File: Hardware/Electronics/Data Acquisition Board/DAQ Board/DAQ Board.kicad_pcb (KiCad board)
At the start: 4 copper layers, 94.7 x 58.9 mm, 131 parts, among them J1 Conn_01x09_Male, J2 USB_B_Mini, J3 Battery Connector, J4 DC Barrel Jack, J5 HC-05 BT Module, J6 ICSP Header, Q1 DMP2100U, SW1 DIP, SW10 SW_SPDT, SW11 SW_SPDT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

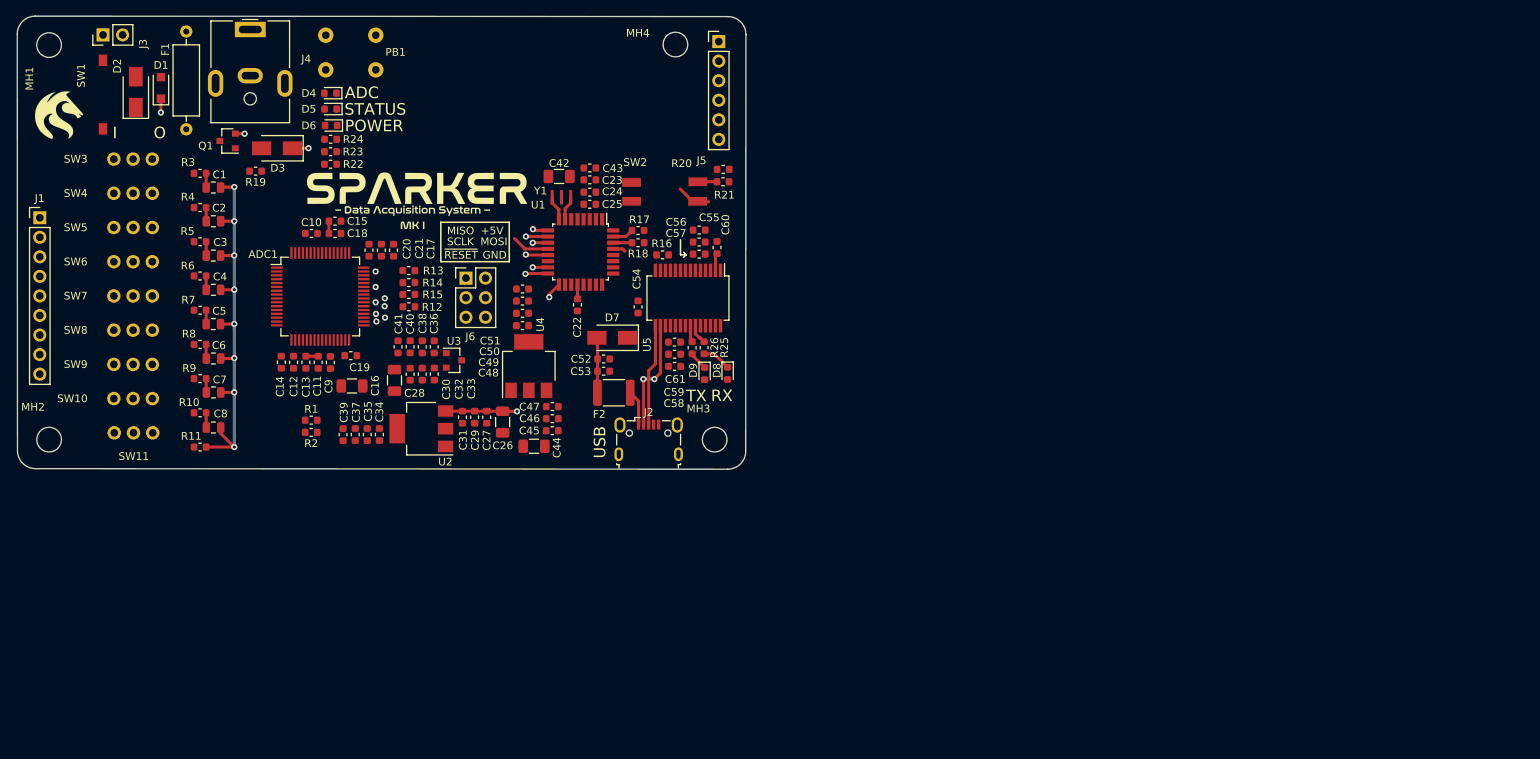
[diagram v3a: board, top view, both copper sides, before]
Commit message: About to start routing traces
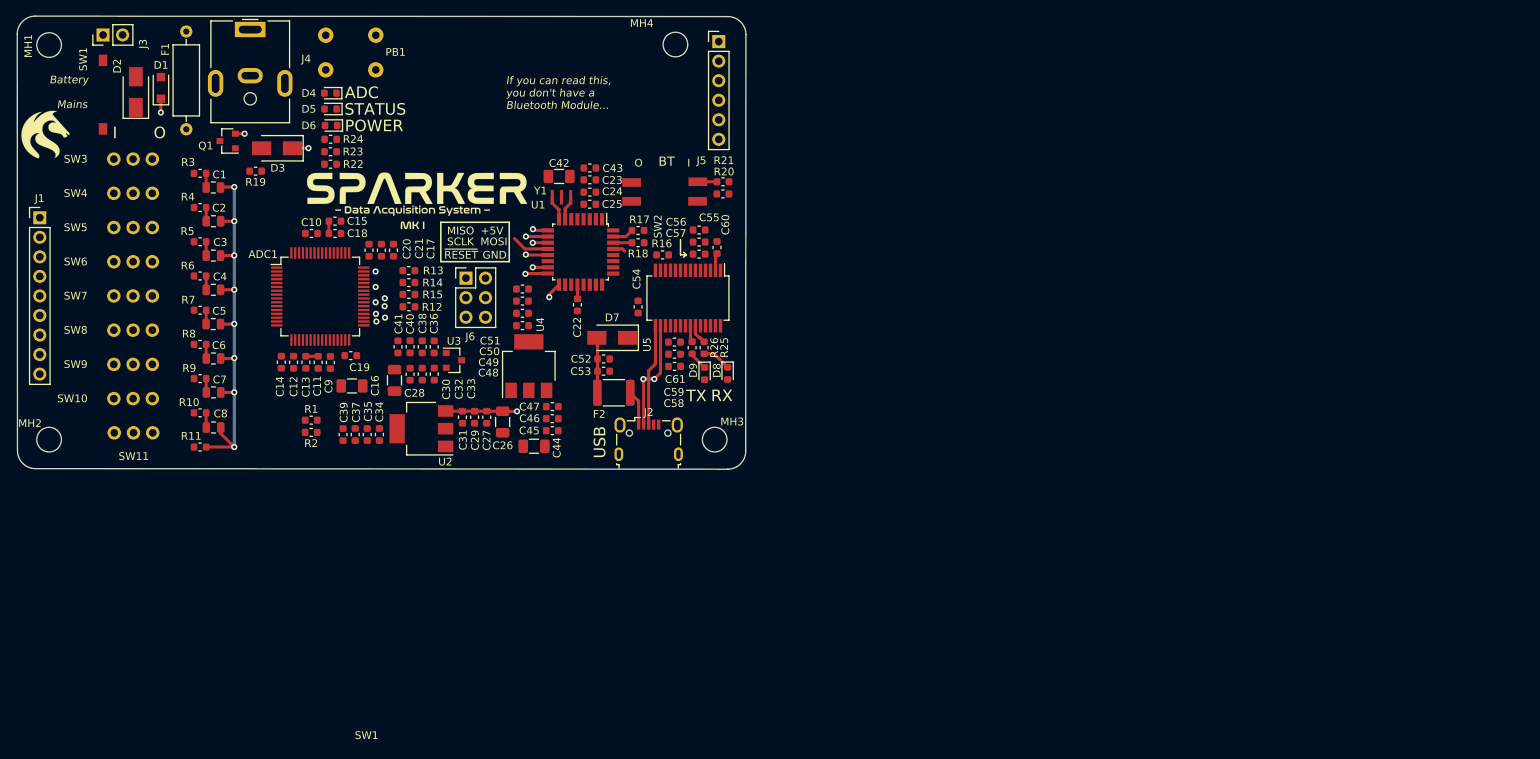
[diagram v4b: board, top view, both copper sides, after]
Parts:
- added ?: , , F.Cu at (24.7, 74.8)
- moved R20 3.19 mm to (110.4, 88.5)
- moved LOGO1 3.08 mm to (22.3, 80.9)
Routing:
- net /HC05_TX: track 2.90 -> 0.00 mm
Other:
- board text added: "BT"
- board text added: "Battery"
- board text added: "If you can read this, you don't have a Bluetooth Module..."
- board text added: "Mains"
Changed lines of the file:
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@@
   (general
     (thickness 1.6)
-    (drawings 31)
-    (tracks 152)
+    (drawings 37)
+    (tracks 150)
     (zones 0)
-    (modules 131)
+    (modules 132)
     (nets 115)
   )
@@
     (visible_elements 7FFFF7FF)
     (pcbplotparams
-      (layerselection 0x010fc_ffffffff)
+      (layerselection 0x090fc_fffffff9)
       (usegerberextensions false)
       (usegerberattributes false)
@@
       (padsonsilk false)
       (subtractmaskfromsilk false)
-      (outputformat 1)
+      (outputformat 4)
       (mirror false)
-      (drillshape 1)
+      (drillshape 0)
       (scaleselection 1)
-      (outputdirectory ""))
+      (outputdirectory "PDFs/"))
   )
   (net 0 "")
@@
     (add_net "Net-(U5-Pad9)")
   )
+  (module "" (layer F.Cu)
+    (at 24.71 74.85)
+    (fp_text reference "" (at 36.25 83.995) (layer F.SilkS)
+      (effects (font (size 1.27 1.27) (thickness 0.15)))
+    )
+    (fp_text value "" (at 36.25 83.995) (layer F.SilkS)
+      (effects (font (size 1.27 1.27) (thickness 0.15)))
+    )
+    (fp_text user SW1 (at 39.38 84.015) (layer F.SilkS)
+      (effects (font (size 1 1) (thickness 0.15)))
+    )
+  )
   (module Switches:SPDT-THT_Slide (layer F.Cu)
     (at 36.25 83.995 180)
@@
     (tags "mounting hole 3.2mm no annular m3")
     (attr virtual)
-    (fp_text reference MH4 (at -4.88 -1.49) (layer F.SilkS)
+    (fp_text reference MH4 (at -4.38 -2.75) (layer F.SilkS)
       (effects (font (size 1 1) (thickness 0.15)))
     )
@@
     (tags "mounting hole 3.2mm no annular m3")
     (attr virtual)
-    (fp_text reference MH3 (at -2.11 -4.01) (layer F.SilkS)
+    (fp_text reference MH3 (at 2.27 -2.32) (layer F.SilkS)
       (effects (font (size 1 1) (thickness 0.15)))
     )
@@
     (tags "mounting hole 3.2mm no annular m3")
     (attr virtual)
-    (fp_text reference MH2 (at -2.09 -4.22) (layer F.SilkS)
+    (fp_text reference MH2 (at -2.48 -2.1) (layer F.SilkS)
       (effects (font (size 1 1) (thickness 0.15)))
     )
@@
     (tags "mounting hole 3.2mm no annular m3")
     (attr virtual)
-    (fp_text reference MH1 (at -2.53 4.37 90) (layer F.SilkS)
+    (fp_text reference MH1 (at -2.68 0.13 90) (layer F.SilkS)
       (effects (font (size 1 1) (thickness 0.15)))
     )
@@
   )
   (module Sparker:UoN (layer F.Cu)
-    (at 24.1 78.34)
+    (at 22.34 80.87)
     (fp_text reference LOGO1 (at 0 0) (layer F.SilkS) hide
       (effects (font (size 1.524 1.524) (thickness 0.3)))
@@
   (module Switches:DIP-Switch_01x01 (layer F.Cu)
     (at 29.84 80.07 90)
-    (fp_text reference SW1 (at 6.93 -2.82 90) (layer F.SilkS)
+    (fp_text reference SW1 (at 9.05 -2.55 90) (layer F.SilkS)
       (effects (font (size 1 1) (thickness 0.15)))
     )
@@
   (module Switches:DIP-Switch_01x02 (layer F.Cu)
     (at 98.512327 86.936407)
-    (fp_text reference SW2 (at 0.47 -2.52) (layer F.SilkS)
+    (fp_text reference SW2 (at 3.437673 5.803593 90) (layer F.SilkS)
       (effects (font (size 1 1) (thickness 0.15)))
     )
@@
   )
   (module Resistor_SMD:R_0603_1608Metric (layer F.Cu)
-    (at 110.41 85.33)
+    (at 110.38 88.52)
     (descr "Resistor SMD 0603 (1608 Metric), square (rectangular) end terminal, IPC_7351 nominal, (Body size source: http://www.tortai-tech.com/upload/download/2011102023233369053.pdf), generated with kicad-footprint-generator")
     (tags resistor)
     (attr smd)
-    (fp_text reference R20 (at -5.4 -0.77) (layer F.SilkS)
+    (fp_text reference R20 (at 0.14 -2.88 180) (layer F.SilkS)
       (effects (font (size 1 1) (thickness 0.15)))
     )
@@
     (tags resistor)
     (attr smd)
-    (fp_text reference R21 (at -0.177673 -1.713593 180) (layer F.SilkS)
+    (fp_text reference R21 (at -0.107673 2.766407 180) (layer F.SilkS)
       (effects (font (size 1 1) (thickness 0.15)))
     )
@@
       (net 89 "Net-(U1-Pad7)"))
   )
+  (gr_text BT (at 101.99 84.31) (layer F.SilkS)
+    (effects (font (size 1.2 1.2) (thickness 0.2)) (justify left))
+  )
+  (gr_text O (at 98.88 84.5) (layer F.SilkS)
+    (effects (font (size 1 1) (thickness 0.15)) (justify left))
+  )
+  (gr_text I (at 105.74 84.5) (layer F.SilkS)
+    (effects (font (size 1 1) (thickness 0.15)) (justify left))
+  )
+  (gr_text Mains (at 27.84 76.9) (layer F.SilkS)
+    (effects (font (size 1 1) (thickness 0.15) italic) (justify right))
+  )
+  (gr_text Battery (at 27.95 73.69) (layer F.SilkS)
+    (effects (font (size 1 1) (thickness 0.15) italic) (justify right))
+  )
+  (gr_text "If you can read this, \nyou don't have a\nBluetooth Module..." (at 82.19 75.4) (layer F.SilkS)
+    (effects (font (size 1 1) (thickness 0.15) italic) (justify left))
+  )
   (gr_line (start 73.73 97.32) (end 82.62 97.32) (layer F.SilkS) (width 0.2))
   (gr_line (start 73.73 92.2) (end 73.73 97.32) (layer F.SilkS) (width 0.2))
@@
   (segment (start 89.08 90.53) (end 89.03 90.53) (width 0.4) (layer F.Cu) (net 90))
   (segment (start 89.08 91.81) (end 89.08 90.53) (width 0.4) (layer F.Cu) (net 90))
-  (segment (start 107.857327 89.536407) (end 108.512327 89.536407) (width 0.4) (layer F.Cu) (net 112))
-  (segment (start 104.839999 87.889079) (end 106.427327 89.476407) (width 0.4) (layer F.Cu) (net 112))
 )

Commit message: Kineses Board layout finished, about to start routing
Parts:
- removed ?: , 
- moved C17 3.22 mm to (64.4, 95.8)
- moved C44 3.05 mm to (88.9, 121.3), turned to 0 degrees
- moved C20 1.54 mm to (65.9, 95.8)
- moved C21 1.54 mm to (67.5, 95.8)
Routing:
- net Net-(J1-Pad9): track 0.00 -> 13.9 mm
- net Net-(J1-Pad1): track 0.00 -> 13.5 mm
- net Net-(J1-Pad8): track 0.08 -> 12.1 mm
- net Net-(J1-Pad2): track 0.00 -> 12.0 mm
- net Net-(J1-Pad7): track 0.00 -> 11.2 mm
- net Net-(J1-Pad3): track 0.00 -> 11.2 mm
- net /ADC1299/AVDD: track 0.00 -> 11.0 mm
- net Net-(D4-Pad2): track 0.00 -> 10.9 mm
- net /VIN_RAW: track 0.00 -> 10.7 mm
- net Net-(J1-Pad6): track 0.00 -> 10.4 mm
- net Net-(J1-Pad4): track 0.00 -> 10.4 mm
- net Net-(J1-Pad5): track 0.00 -> 9.62 mm
- net Net-(R7-Pad2): track 0.00 -> 8.69 mm
- net Net-(R5-Pad2): track 0.00 -> 8.69 mm
- net Net-(R6-Pad2): track 0.00 -> 8.69 mm
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- added copper zone on In1.Cu, net /GND
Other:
- net class Default: clearance 0.2 -> 0.15; trace_width 0.4 -> 0.3
- net class High_Current added: clearance 0.2, trace_width 0.8, via_dia 1, via_drill 0.8
- rule trace_clearance: 0.2 -> 0.15

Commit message: Routing Finished
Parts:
- moved C21 101.3 mm to (168.8, 99.0)
- moved C20 101.3 mm to (167.2, 99.0)
- moved C11 99.9 mm to (157.6, 113.6)
- moved C28 99.9 mm to (167.5, 115.9)
- moved C30 99.9 mm to (169.6, 115.1)
- moved C40 99.9 mm to (169.6, 111.6)
- moved C45 99.9 mm to (188.0, 122.5)
- moved C55 99.9 mm to (207.1, 96.4)
- moved C56 99.9 mm to (207.1, 98.0)
- moved C57 99.9 mm to (207.1, 99.5)
- moved D8 99.9 mm to (210.8, 115.0)
- moved J2 99.9 mm to (200.5, 123.6)
- moved J6 99.9 mm to (176.8, 102.7)
- moved MH4 99.9 mm to (204.0, 72.3)
- moved ADC1 99.9 mm to (157.9, 105.0)
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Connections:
- J5 pad 1: /AT_COMM -> Net-(J5-Pad1)
- U1 pad 32: /AT_COMM -> Net-(U1-Pad32)
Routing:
- net /ADC1299/~RESET: track 1.64 -> 84.5 mm, vias 1 -> 3
- net /+5V: track 0.00 -> 63.9 mm, vias 0 -> 10
- net /ADC1299/AVDD: track 11.0 -> 68.0 mm, vias 0 -> 7
- net /ADC1299/~PWDN: track 2.00 -> 37.5 mm
- net /ADC1299/MID_SUPPLY: track 0.00 -> 33.1 mm, vias 0 -> 2
- net /ADC1299/START: track 1.96 -> 31.4 mm
- net Net-(R23-Pad2): track 4.88 -> 32.7 mm
- net /ADC1299/~CS: track 2.88 -> 28.8 mm
- net /ADC1299/MOSI: track 1.96 -> 27.2 mm, vias 2 -> 1
- net /ADC1299/SCLK: track 2.15 -> 26.9 mm, vias 2 -> 1
- net /Arduino Nano/RX: track 0.00 -> 24.3 mm, vias 0 -> 2
- net /ADC1299/MISO: track 2.93 -> 26.5 mm, vias 2 -> 1
- net /ADC1299/~DRDY: track 2.85 -> 25.8 mm
- net /ADC1299/DVDD: track 0.00 -> 22.0 mm, vias 0 -> 2
- net Net-(ADC1-Pad2): track 1.84 -> 20.7 mm
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- added copper zone on In2.Cu, net /+5V
- added copper zone on In2.Cu, net /ADC1299/AVDD
- added copper zone on In2.Cu, net /ADC1299/DVDD
- added copper zone on B.Cu, net /GND
- added copper zone on F.Cu, net /GND
- added copper zone on In2.Cu, net /VIN
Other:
- net class Fine_Pitch added: clearance 0.15, trace_width 0.25, via_dia 0.8, via_drill 0.4
- net class High_Current: via_dia 1 -> 0.8; via_drill 0.8 -> 0.4
- net class Mid_Current added: clearance 0.15, trace_width 0.5, via_dia 0.8, via_drill 0.4

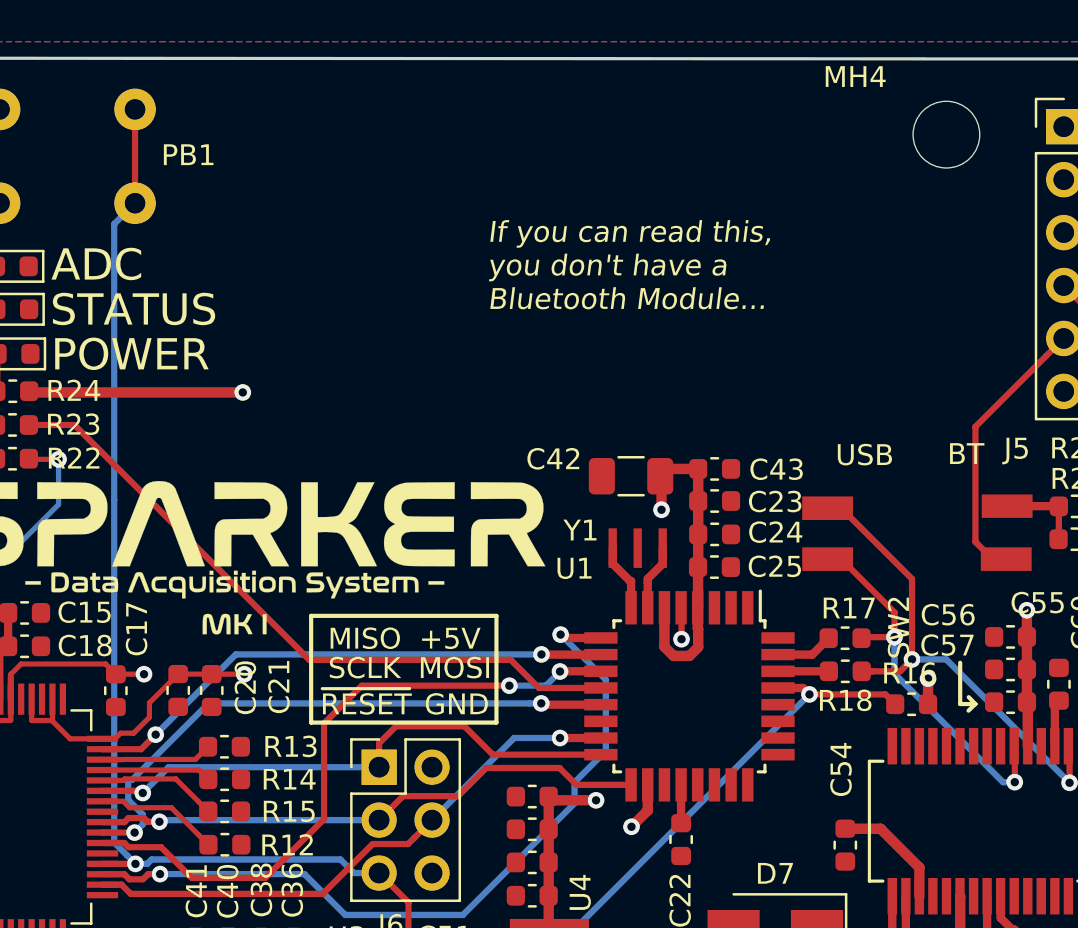
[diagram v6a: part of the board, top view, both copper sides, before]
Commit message: Changed 5V regulators for LDOs, changed datasheet for 100u tantalum cap
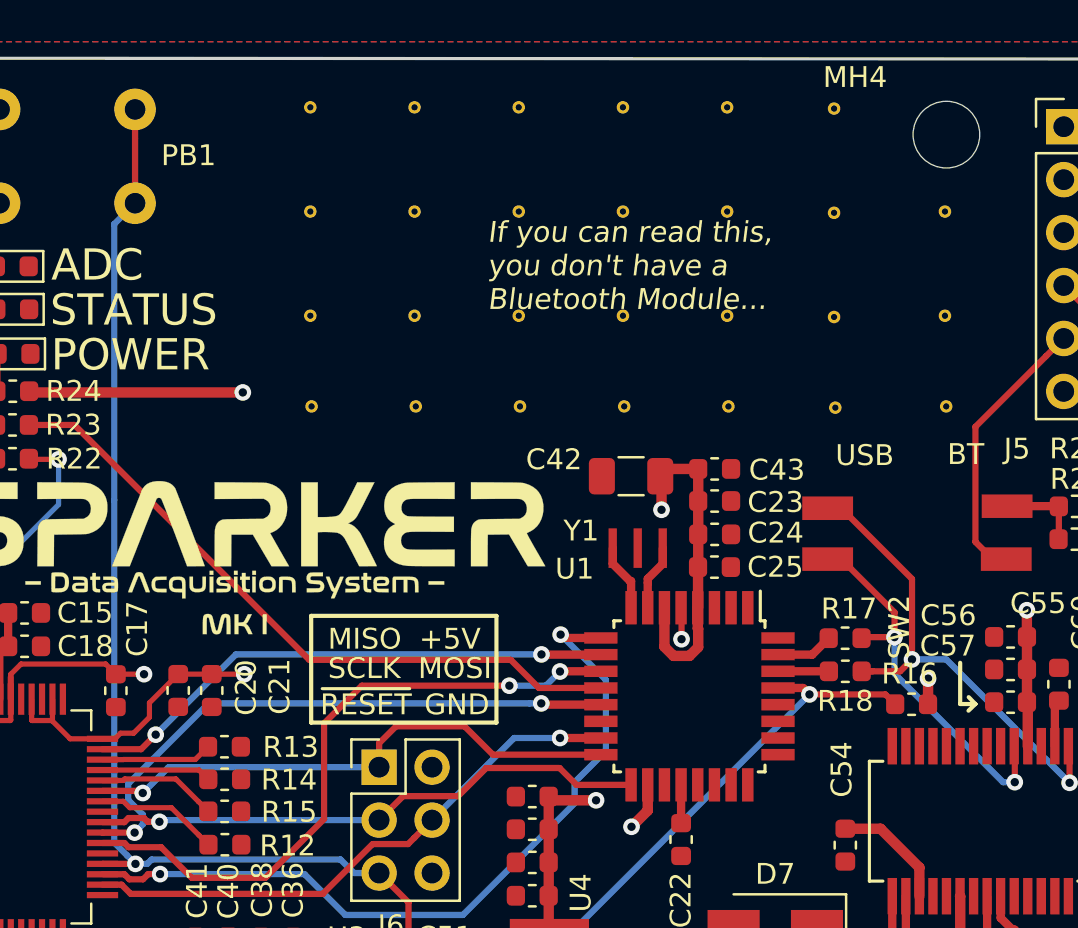
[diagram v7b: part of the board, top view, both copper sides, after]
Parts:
- added ?: , Vias:VIA-0.6mm, F.Cu at (204.0, 85.3)
- added ?: , Vias:VIA-0.6mm, F.Cu at (173.6, 85.3)
- added ?: , Vias:VIA-0.6mm, F.Cu at (193.6, 85.3)
- added ?: , Vias:VIA-0.6mm, F.Cu at (183.6, 85.3)
- added ?: , Vias:VIA-0.6mm, F.Cu at (193.5, 81.0)
- added ?: , Vias:VIA-0.6mm, F.Cu at (188.5, 81.0)
- added ?: , Vias:VIA-0.6mm, F.Cu at (183.5, 81.0)
- added ?: , Vias:VIA-0.6mm, F.Cu at (178.5, 81.0)
- added ?: , Vias:VIA-0.6mm, F.Cu at (173.5, 81.0)
- added ?: , Vias:VIA-0.6mm, F.Cu at (193.5, 76.0)
- added ?: , Vias:VIA-0.6mm, F.Cu at (188.5, 76.0)
- added ?: , Vias:VIA-0.6mm, F.Cu at (203.9, 81.0)
- added ?: , Vias:VIA-0.6mm, F.Cu at (183.5, 76.0)
- added ?: , Vias:VIA-0.6mm, F.Cu at (178.5, 76.0)
- added ?: , Vias:VIA-0.6mm, F.Cu at (173.5, 76.0)
- added ?: , Vias:VIA-0.6mm, F.Cu at (193.5, 71.0)
- added ?: , Vias:VIA-0.6mm, F.Cu at (188.5, 71.0)
- added ?: , Vias:VIA-0.6mm, F.Cu at (183.5, 71.0)
- added ?: , Vias:VIA-0.6mm, F.Cu at (178.5, 71.0)
- added ?: , Vias:VIA-0.6mm, F.Cu at (173.5, 71.0)
- added ?: , Vias:VIA-0.6mm, F.Cu at (203.9, 76.0)
- added ?: , Vias:VIA-0.6mm, F.Cu at (198.7, 85.4)
- added ?: , Vias:VIA-0.6mm, F.Cu at (198.6, 71.0)
- added ?: , Vias:VIA-0.6mm, F.Cu at (198.6, 81.0)
- added ?: , Vias:VIA-0.6mm, F.Cu at (198.6, 76.0)
- added ?: , Vias:VIA-0.6mm, F.Cu at (188.6, 85.3)
- added ?: , Vias:VIA-0.6mm, F.Cu at (178.6, 85.3)
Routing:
- net /ADC1299/DVDD: track 22.0 -> 37.8 mm
- removed copper zone on In2.Cu, net /ADC1299/DVDD
